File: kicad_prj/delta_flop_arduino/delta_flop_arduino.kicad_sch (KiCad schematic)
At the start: 1 part, among them U1 Arduino_Nano

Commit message: Pre-version made
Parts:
- added D1: Floppy Connector, Connector_IDC:IDC-Header_2x17_P2.54mm_Vertical, symbol delta_flop_pre:34_pin_floppy_convertor
- added J1: SD_Card, delta_flop_pre:SDCARD_4UCONN, symbol delta_flop_pre:SD_Card
- added J2: SCREEN OUTPUT, Connector_PinHeader_2.54mm:PinHeader_1x04_P2.54mm_Vertical, symbol delta_flop_pre:Conn_01x04
- added J3: Power Input (5V), Connector_PinHeader_2.54mm:PinHeader_1x02_P2.54mm_Vertical, symbol Connector_Generic:Conn_01x02
- added JP1: Jumper_3_Open, Connector_PinHeader_2.54mm:PinHeader_1x03_P2.54mm_Vertical, symbol Jumper:Jumper_3_Open
- added R1: 10K, R_Axial_DIN0207_L6.3mm_D2.5mm_P10.16mm_Horizontal, symbol Device:R
- added R2, R3, R4: 3.3K, R_Axial_DIN0207_L6.3mm_D2.5mm_P10.16mm_Horizontal, symbol Device:R
- added R5, R6, R7: 2.2K, R_Axial_DIN0207_L6.3mm_D2.5mm_P10.16mm_Horizontal, symbol Device:R
- added SW1: RotaryEncoder_Switch, Rotary_Encoder:RotaryEncoder_Alps_EC11E-Switch_Vertical_H20mm, symbol delta_flop_pre:RotaryEncoder_Switch
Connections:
- net at U1.1 (D1/TX): now also D1.30 (READ_DATA)
- net at U1.10 (D7): now also JP1.2 (C)
- net at U1.11 (D8): now also D1.8 (INDEX)
- net SS: now reaches U1.13 (~D10)
- net SS: now also R7.1
- net MOSI: now reaches U1.14 (~D11)
- net MOSI: now also R6.1
- net MISO: now reaches U1.15 (D12)
- net MISO: now also J1.7 (DAT0), R1.2
- net SCK: now reaches U1.16 (D13)
- net SCK: now also R5.1
- net 3.3V: now reaches U1.17 (3V3)
- net 3.3V: now also J1.4 (VDD), R1.1
- net at U1.2 (D0/RX): now also D1.32 (HEAD_SELECT)
- net at U1.20 (A1/D15): now also SW1.S1
- net at U1.21 (A2/D16): now also SW1.A
- net at U1.22 (A3/D17): now also SW1.B
- net at U1.23 (A4/D18): now also J2.3 (Pin_3)
- net at U1.24 (A5/D19): now also J2.4 (Pin_4)
- net 5V: now reaches U1.27 (+5V)
- net 5V: now also J2.2 (Pin_2), J3.1 (Pin_1)
- net GND: now reaches U1.29 (GND)
- net GND: now also U1.4 (GND), D1.1 (GND), D1.11 (GND), D1.13 (GND), D1.15 (GND), D1.17 (GND), D1.19 (GND), D1.21 (GND), D1.23 (GND), D1.25 (GND), D1.27 (GND), D1.29 (GND), D1.3 (GND), D1.31 (GND), D1.33 (GND), D1.5 (GND), D1.7 (GND), D1.9 (GND), J1.12 (SHELL1), J1.13 (SHELL2), J1.3 (VSS), J1.6 (VSS), J2.1 (Pin_1), J3.2 (Pin_2), R2.2, R3.2, R4.2, SW1.C, SW1.S2
- net at U1.5 (D2): now also D1.28 (WRITE_PROTECT)
- net at U1.6 (~D3): now also D1.26 (TRACK)
- net at U1.7 (D4): now also D1.20 (STEP)
- net at U1.8 (~D5): now also D1.18 (DIRECTION)
- net at U1.9 (~D6): now also D1.16 (MOTOR_1)
- new net: J1.5 (CLK), R2.1, R5.2
- new net: J1.2 (CMD), R3.1, R6.2
- new net: D1.12 (DRIVE_SELECT_1), JP1.1 (A)
- new net: D1.10 (MOTOR_0), JP1.3 (B)
- new net: J1.1 (CD/DAT3), R4.1, R7.2
- no-connect marks 0 -> 15
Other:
- moved on the sheet: U1

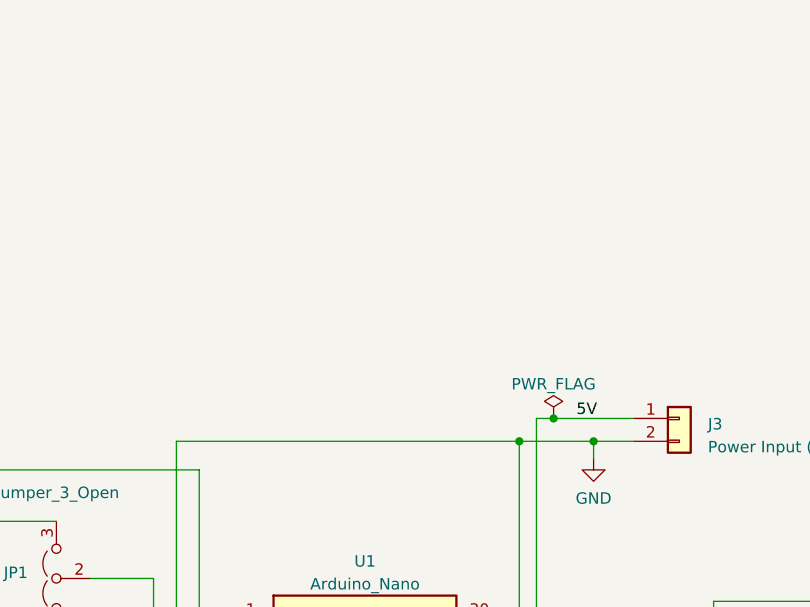
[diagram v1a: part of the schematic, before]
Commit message: Big screen update
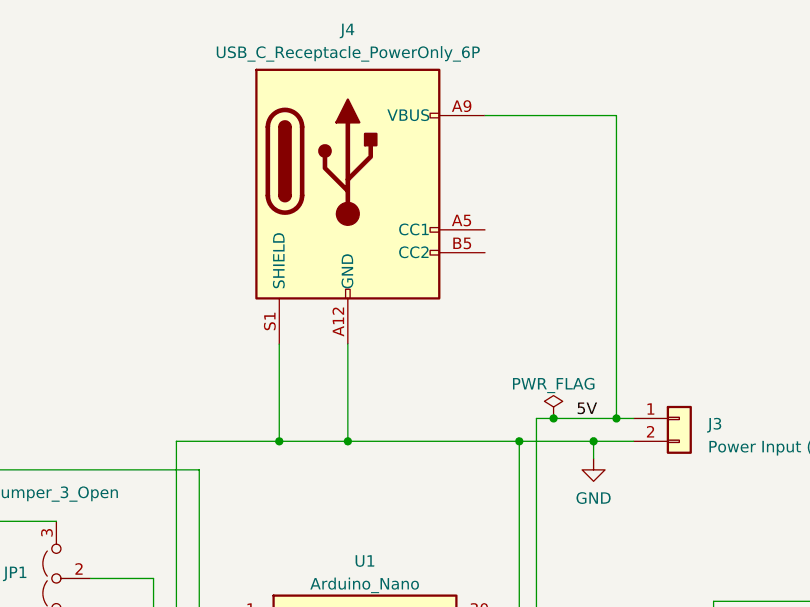
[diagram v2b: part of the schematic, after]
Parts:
- added J4: USB_C_Receptacle_PowerOnly_6P, delta_flop_pre:USB_C_Receptacle_XKB_U262-16XN-4BVC11, symbol Connector:USB_C_Receptacle_PowerOnly_6P
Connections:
- net 5V: now also J4.A9 (VBUS), J4.B9 (VBUS)
- net GND: now also J4.A12 (GND), J4.B12 (GND), J4.S1 (SHIELD)
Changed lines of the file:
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@@
   (junction (at 61.595 139.7) (diameter 0) (color 0 0 0 0)
   )
+  (junction (at 138.43 99.06) (diameter 0) (color 0 0 0 0)
+  )
   (junction (at 127.635 101.6) (diameter 0) (color 0 0 0 0)
   )
@@
   (junction (at 194.945 137.16) (diameter 0) (color 0 0 0 0)
   )
+  (junction (at 100.965 101.6) (diameter 0) (color 0 0 0 0)
+  )
   (junction (at 131.445 99.06) (diameter 0) (color 0 0 0 0)
   )
@@
   )
   (junction (at 129.54 128.905) (diameter 0) (color 0 0 0 0)
+  )
+  (junction (at 108.585 101.6) (diameter 0) (color 0 0 0 0)
   )
   (junction (at 181.61 139.7) (diameter 0) (color 0 0 0 0)
@@
     (stroke (width 0) (type default))
   )
+  (wire (pts (xy 100.965 101.6) (xy 108.585 101.6))
+    (stroke (width 0) (type default))
+  )
   (wire (pts (xy 95.25 136.525) (xy 71.755 136.525))
     (stroke (width 0) (type default))
@@
     (stroke (width 0) (type default))
   )
+  (wire (pts (xy 108.585 101.6) (xy 127.635 101.6))
+    (stroke (width 0) (type default))
+  )
   (wire (pts (xy 61.595 129.54) (xy 61.595 134.62))
     (stroke (width 0) (type default))
@@
     (stroke (width 0) (type default))
   )
+  (wire (pts (xy 100.965 90.805) (xy 100.965 101.6))
+    (stroke (width 0) (type default))
+  )
   (wire (pts (xy 67.31 110.49) (xy 67.31 116.84))
     (stroke (width 0) (type default))
@@
     (stroke (width 0) (type default))
   )
-  (wire (pts (xy 140.335 99.06) (xy 131.445 99.06))
+  (wire (pts (xy 140.335 99.06) (xy 138.43 99.06))
     (stroke (width 0) (type default))
   )
@@
     (stroke (width 0) (type default))
   )
-  (wire (pts (xy 89.535 101.6) (xy 127.635 101.6))
+  (wire (pts (xy 89.535 101.6) (xy 100.965 101.6))
     (stroke (width 0) (type default))
   )
@@
     (stroke (width 0) (type default))
   )
+  (wire (pts (xy 123.825 65.405) (xy 138.43 65.405))
+    (stroke (width 0) (type default))
+  )
   (wire (pts (xy 175.26 132.08) (xy 175.26 147.955))
     (stroke (width 0) (type default))
@@
     (stroke (width 0) (type default))
   )
+  (wire (pts (xy 108.585 90.805) (xy 108.585 101.6))
+    (stroke (width 0) (type default))
+  )
   (wire (pts (xy 173.99 139.7) (xy 181.61 139.7))
     (stroke (width 0) (type default))
@@
     (stroke (width 0) (type default))
   )
+  (wire (pts (xy 138.43 99.06) (xy 131.445 99.06))
+    (stroke (width 0) (type default))
+  )
   (wire (pts (xy 165.1 139.7) (xy 166.37 139.7))
     (stroke (width 0) (type default))
@@
   )
   (wire (pts (xy 57.785 157.48) (xy 74.295 157.48))
+    (stroke (width 0) (type default))
+  )
+  (wire (pts (xy 138.43 65.405) (xy 138.43 99.06))
     (stroke (width 0) (type default))
   )
@@
         )
       )
+    )
+  )
+  (symbol (lib_id "Connector:USB_C_Receptacle_PowerOnly_6P") (at 108.585 73.025 0) (unit 1)
+    (in_bom yes) (on_board yes) (dnp no) (fields_autoplaced)
+    (property "Reference" "J4" (at 108.585 55.88 0)
+      (effects (font (size 1.27 1.27)))
+    )
+    (property "Value" "USB_C_Receptacle_PowerOnly_6P" (at 108.585 58.42 0)
+      (effects (font (size 1.27 1.27)))
+    )
+    (property "Footprint" "delta_flop_pre:USB_C_Receptacle_XKB_U262-16XN-4BVC11" (at 112.395 70.485 0)
+      (effects (font (size 1.27 1.27)) hide)
+    )
+    (property "Datasheet" "https://www.usb.org/sites/default/files/documents/usb_type-c.zip" (at 108.585 73.025 0)
+      (effects (font (size 1.27 1.27)) hide)
+    )
+    (pin "A12")
+    (pin "A5")
+    (pin "A9")
+    (pin "B12")
+    (pin "B5")
+    (pin "B9")
+    (pin "S1")
+    (instances
+      (project "delta_flop_arduino"
+        (path "/6217fe07-62c2-46a3-8b7c-e98338e65dc8"
+          (reference "J4") (unit 1)
+        )
+      )

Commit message: Small fixes
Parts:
- added C1: 0.1uF, Capacitor_THT:C_Disc_D7.0mm_W2.5mm_P5.00mm, symbol Device:C
- R1: renamed from R6; footprint R_Axial_DIN0207_L6.3mm_D2.5mm_P10.16mm_Horizontal -> Resistor_THT:R_Axial_DIN0207_L6.3mm_D2.5mm_P10.16mm_Horizontal
- R2: renamed from R7; footprint R_Axial_DIN0207_L6.3mm_D2.5mm_P10.16mm_Horizontal -> Resistor_THT:R_Axial_DIN0207_L6.3mm_D2.5mm_P10.16mm_Horizontal
- R3: renamed from R5; footprint R_Axial_DIN0207_L6.3mm_D2.5mm_P10.16mm_Horizontal -> Resistor_THT:R_Axial_DIN0207_L6.3mm_D2.5mm_P10.16mm_Horizontal
- R4: renamed from R2; footprint R_Axial_DIN0207_L6.3mm_D2.5mm_P10.16mm_Horizontal -> Resistor_THT:R_Axial_DIN0207_L6.3mm_D2.5mm_P10.16mm_Horizontal
- R5: renamed from R1; footprint R_Axial_DIN0207_L6.3mm_D2.5mm_P10.16mm_Horizontal -> Resistor_THT:R_Axial_DIN0207_L6.3mm_D2.5mm_P10.16mm_Horizontal
- R6: renamed from R4; footprint R_Axial_DIN0207_L6.3mm_D2.5mm_P10.16mm_Horizontal -> Resistor_THT:R_Axial_DIN0207_L6.3mm_D2.5mm_P10.16mm_Horizontal
- R7: renamed from R3; footprint R_Axial_DIN0207_L6.3mm_D2.5mm_P10.16mm_Horizontal -> Resistor_THT:R_Axial_DIN0207_L6.3mm_D2.5mm_P10.16mm_Horizontal
- renumbered J2 to J1, J1 to J2
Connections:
- net 5V: now also C1.1
- net GND: now also C1.2

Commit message: Version 1.1 Update
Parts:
- removed J3: Power Input (5V), Connector_PinHeader_2.54mm:PinHeader_1x02_P2.54mm_Vertical, symbol Connector_Generic:Conn_01x02
- removed J4: USB_C_Receptacle_PowerOnly_6P, delta_flop_pre:USB_C_Receptacle_XKB_U262-16XN-4BVC11, symbol Connector:USB_C_Receptacle_PowerOnly_6P
- added J3: Power connector, delta_flop_pre:USB-C Power board, symbol Connector_Generic:Conn_01x04
- added SW2: Right, Button_Switch_THT:SW_PUSH_6mm, symbol Switch:SW_Push
- added SW3: Left, Button_Switch_THT:SW_PUSH_6mm, symbol Switch:SW_Push
- added SW4: Enter, Button_Switch_THT:SW_PUSH_6mm, symbol Switch:SW_Push
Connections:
- net 5V: now also J3.1 (Pin_1); no longer C1.1
- net GND: now also C1.1, J3.4 (Pin_4), SW2.2, SW3.2, SW4.2
- net at SW1.S1, U1.20 (A1/D15): now also SW4.1
- net at SW1.A, U1.21 (A2/D16): now also SW2.1
- net at SW1.B, U1.22 (A3/D17): now also SW3.1
- no-connect marks 15 -> 19

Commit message: New version
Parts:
- removed C1: 0.1uF, Capacitor_THT:C_Disc_D7.0mm_W2.5mm_P5.00mm, symbol Device:C
- removed D1: Floppy Connector, Connector_IDC:IDC-Header_2x17_P2.54mm_Vertical, symbol delta_flop_pre:34_pin_floppy_convertor
- removed J1: SCREEN OUTPUT, Connector_PinHeader_2.54mm:PinHeader_1x04_P2.54mm_Vertical, symbol delta_flop_pre:Conn_01x04
- removed J2: SD_Card, delta_flop_pre:SDCARD_4UCONN, symbol delta_flop_pre:SD_Card
- removed J3: Power connector, delta_flop_pre:USB-C Power board, symbol Connector_Generic:Conn_01x04
- removed JP1: Jumper_3_Open, Connector_PinHeader_2.54mm:PinHeader_1x03_P2.54mm_Vertical, symbol Jumper:Jumper_3_Open
- removed R1, R2, R3: 2.2K, Resistor_THT:R_Axial_DIN0207_L6.3mm_D2.5mm_P10.16mm_Horizontal, symbol Device:R
- removed R4, R6, R7: 3.3K, Resistor_THT:R_Axial_DIN0207_L6.3mm_D2.5mm_P10.16mm_Horizontal, symbol Device:R
- removed R5: 10K, Resistor_THT:R_Axial_DIN0207_L6.3mm_D2.5mm_P10.16mm_Horizontal, symbol Device:R
- removed SW1: RotaryEncoder_Switch, Rotary_Encoder:RotaryEncoder_Alps_EC11E-Switch_Vertical_H20mm, symbol delta_flop_pre:RotaryEncoder_Switch
- removed SW2: Right, Button_Switch_THT:SW_PUSH_6mm, symbol Switch:SW_Push
- removed SW3: Left, Button_Switch_THT:SW_PUSH_6mm, symbol Switch:SW_Push
- removed SW4: Enter, Button_Switch_THT:SW_PUSH_6mm, symbol Switch:SW_Push
- removed U1: Arduino_Nano, delta_flop_pre:Arduino_Nano, symbol delta_flop_pre:Arduino_Nano
- added C1: 0.1uF, Floppy_emu_footprints:C_Disc_D7.0mm_W2.5mm_P5.00mm, symbol floppy_symbols:C
- added D1: Floppy Connector, Floppy_emu_footprints:IDC-Header_2x17_P2.54mm_Vertical, symbol floppy_symbols:34_pin_floppy_convertor
- added J1: SCREEN OUTPUT, Floppy_emu_footprints:PinHeader_1x04_P2.54mm_Vertical, symbol floppy_symbols:Conn_01x04
- added J2: SD_Card, Floppy_emu_footprints:SDCARD_4UCONN, symbol floppy_symbols:SD_Card
- added J3: Power connector, Floppy_emu_footprints:USB-C Power board, symbol floppy_symbols:Conn_01x04
- added JP1: Jumper_3_Open, Floppy_emu_footprints:PinHeader_1x03_P2.54mm_Vertical, symbol floppy_symbols:Jumper_3_Open
- added R1, R4, R5: 3.3K, Floppy_emu_footprints:R_Axial_DIN0207_L6.3mm_D2.5mm_P10.16mm_Horizontal, symbol floppy_symbols:R
- added R2: 10K, Floppy_emu_footprints:R_Axial_DIN0207_L6.3mm_D2.5mm_P10.16mm_Horizontal, symbol floppy_symbols:R
- added R3, R6, R7: 2.2K, Floppy_emu_footprints:R_Axial_DIN0207_L6.3mm_D2.5mm_P10.16mm_Horizontal, symbol floppy_symbols:R
- added SW1: Right, Floppy_emu_footprints:SW_PUSH_6mm, symbol floppy_symbols:SW_Push
- added SW2: Enter, Floppy_emu_footprints:SW_PUSH_6mm, symbol floppy_symbols:SW_Push
- added SW3: Left, Floppy_emu_footprints:SW_PUSH_6mm, symbol floppy_symbols:SW_Push
- added U1: Arduino_Nano, w_conn_av:Arduino_Nano, symbol floppy_symbols:Arduino_Nano
- added U2: 7400, Floppy_emu_footprints:DIP-14_W7.62mm_Socket_LongPads, symbol floppy_symbols:7400
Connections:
- net 3.3V: now also J2.4 (VDD), R2.1, U1.17 (3V3)
- net GND: now also C1.2, D1.1 (GND), D1.11 (GND), D1.13 (GND), D1.15 (GND), D1.17 (GND), D1.19 (GND), D1.21 (GND), D1.23 (GND), D1.25 (GND), D1.27 (GND), D1.29 (GND), D1.3 (GND), D1.31 (GND), D1.33 (GND), D1.5 (GND), D1.7 (GND), D1.9 (GND), J1.1 (Pin_1), J2.3 (VSS), J2.6 (VSS), J3.4 (Pin_4), R1.2, R4.2, R5.2, SW1.2, SW2.2, SW3.2, U1.29 (GND), U1.4 (GND), U2.7 (GND)
- net MISO: now also J2.7 (DAT0), R2.2, U1.15 (D12)
- net MOSI: now also R3.2, U1.14 (~D11)
- net SCK: now also R6.2, U1.16 (D13)
- new net: J2.5 (CLK), R1.1, R6.1
- new net: J2.1 (CD/DAT3), R5.1, R7.1
- new net: U1.1 (D1/TX), U2.1, U2.2
- new net: JP1.2 (C), U1.10 (D7)
- new net: SW2.1, U1.20 (A1/D15)
- new net: SW3.1, U1.21 (A2/D16)
- new net: SW1.1, U1.22 (A3/D17)
- new net: U2.3, U2.4, U2.5
- new net: J2.2 (CMD), R3.1, R4.1
- new net: D1.10 (MOTOR_0), JP1.3 (B)
- new net: D1.12 (DRIVE_SELECT_1), JP1.1 (A)
- new net +5V: C1.1, J1.2 (Pin_2), J3.1 (Pin_1), U1.27 (+5V), U2.14 (VCC)
- new net A0: D1.24 (WRITE_GATE), U1.19 (A0/D14)
- new net D10: R7.2, U1.13 (~D10)
- new net D2: D1.28 (WRITE_PROTECT), U1.5 (D2)
- new net D3: D1.26 (TRACK), U1.6 (~D3)
- new net D4: D1.20 (STEP), U1.7 (D4)
- new net D5: D1.18 (DIRECTION), U1.8 (~D5)
- new net D6: D1.16 (MOTOR_1), U1.9 (~D6)
- new net D8: D1.22 (WRITE_DATA), U1.11 (D8)
- new net D9: D1.8 (INDEX), U1.12 (~D9)
- new net RX: D1.32 (HEAD_SELECT), U1.2 (D0/RX)
- new net SCL: J1.4 (Pin_4), U1.24 (A5/D19)
- new net SDA: J1.3 (Pin_3), U1.23 (A4/D18)
- new net TX: D1.30 (READ_DATA), U2.6
- no-connect marks 19 -> 23
